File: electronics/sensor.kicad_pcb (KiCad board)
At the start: 2 copper layers, 98 x 52.8 mm, 3 parts, among them P1 SENSOR, U1 AH1815

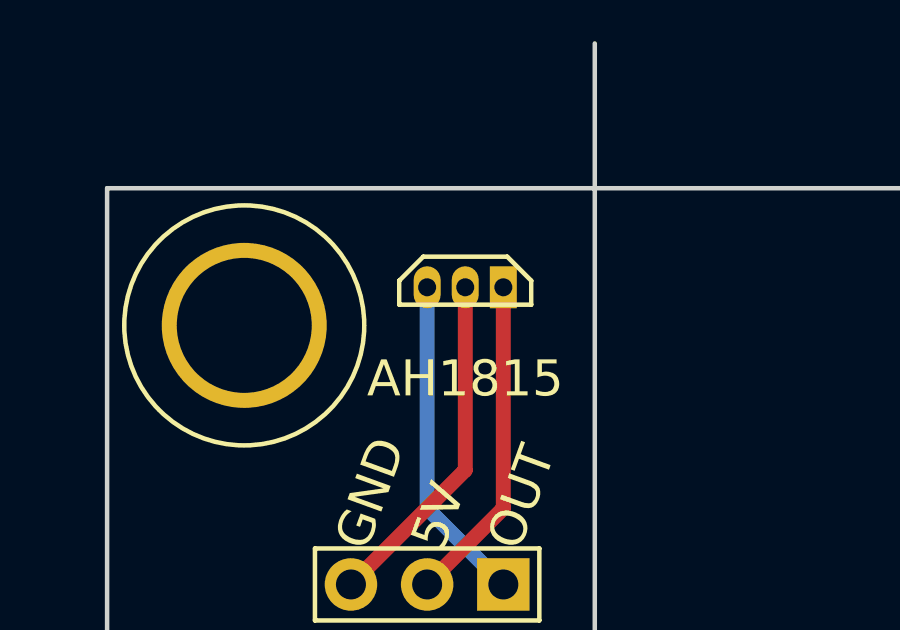
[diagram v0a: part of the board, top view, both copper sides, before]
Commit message: Replace AH1815 references with AH3391Q
The AH1815 hall effect sensor won't work, as it samples the magnetic field too infrequently for the precision needed, as mentioned in https://github.com/scottbez1/splitflap/issues/29#issuecomment-418163631

This replaces the AH1815 schematic/pcb module with a generic "hall_effect" module (since it seems most hall effect sensors have the same pinout and physical dimensions), and updates the schematic reference and BOM to specify AH3391Q as the preferred sensor. As noted in https://github.com/scottbez1/splitflap/issues/29#issuecomment-418234571 a number of other variants of hall effect sensor would also work, besides the AH3391Q, so the PCB silkscreen is now generic ("Hall Effect" instead of "AH1815"), with added pin labels for the hall effect sensor.
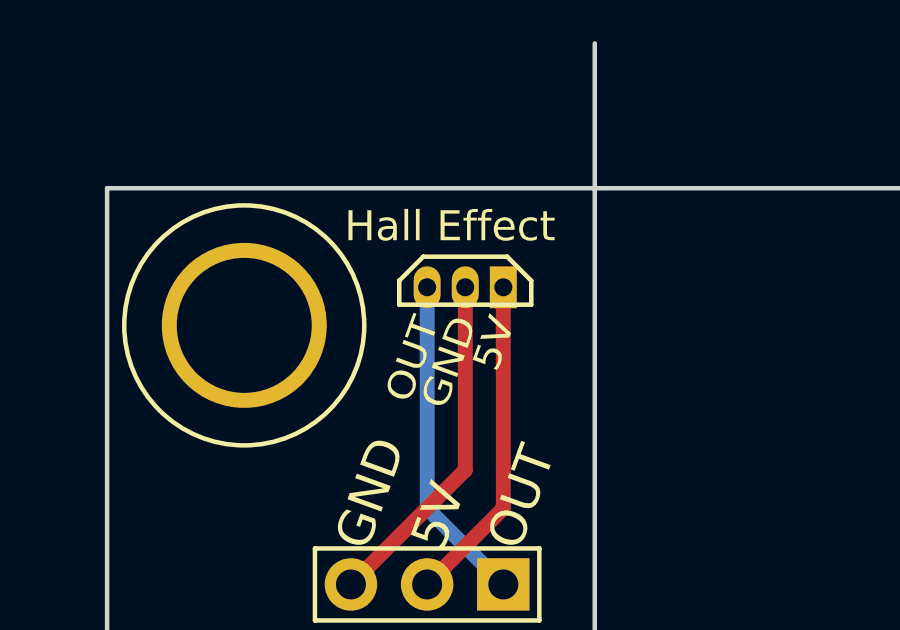
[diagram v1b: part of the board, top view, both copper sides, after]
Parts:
- U1: value AH1815 -> hall_effect; footprint ah1815:AH1815 -> hall_effect:hall_effect
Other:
- board text added: "Hall Effect"
- board text removed: "AH1815"
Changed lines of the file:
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@@
     (links 3)
     (no_connects 0)
-    (area 7.610287 15.098999 116.075001 68.075001)
+    (area 1.514287 7.37 116.075001 68.075001)
     (thickness 1.6)
-    (drawings 15)
+    (drawings 18)
     (tracks 6)
     (zones 0)
@@
       (clearance 1.5))
   )
-  (module ah1815:AH1815 (layer B.Cu)
+  (module hall_effect:hall_effect (layer B.Cu)
     (at 31.938 23.302 180)
     (fp_text reference U1 (at 5.08 1.27 180) (layer B.SilkS) hide
       (effects (font (size 1 1) (thickness 0.15)) (justify mirror))
     )
-    (fp_text value AH1815 (at 0 2.54 180) (layer B.Fab) hide
+    (fp_text value hall_effect (at 0 2.54 180) (layer B.Fab) hide
       (effects (font (size 1 1) (thickness 0.15)) (justify mirror))
     )
@@
       (net 3 "Net-(P1-Pad1)"))
   )
+  (gr_text 5V (at 33.208 24.318 70) (layer F.SilkS)
+    (effects (font (size 0.9 1) (thickness 0.15)) (justify right))
+  )
+  (gr_text GND (at 31.938 24.318 70) (layer F.SilkS)
+    (effects (font (size 0.9 1) (thickness 0.15)) (justify right))
+  )
+  (gr_text OUT (at 30.668 24.318 70) (layer F.SilkS)
+    (effects (font (size 0.9 1) (thickness 0.15)) (justify right))
+  )
   (dimension 8.636 (width 0.3) (layer Cmts.User)
     (gr_text "8.636 mm" (at 28.89 14.92) (layer Cmts.User)
@@
   )
   (gr_line (start 20 20) (end 116 20) (angle 90) (layer Edge.Cuts) (width 0.15))
-  (gr_text AH1815 (at 31.938 26.35) (layer F.SilkS)
-    (effects (font (size 1.2 1.2) (thickness 0.24)))
+  (gr_text "Hall Effect" (at 31.43 21.27) (layer F.SilkS)
+    (effects (font (size 1 1) (thickness 0.15)))
   )
   (gr_text OUT (at 33.208 31.938 70) (layer F.SilkS)

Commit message: Change sensor references to U100/P100 to avoid confusion with U1/P1 on controller PCB
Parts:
- U100: renamed from U1; value hall_effect -> AH3391Q
- renumbered P1 to P100
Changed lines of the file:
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@@
     (links 3)
     (no_connects 0)
-    (area 1.514287 7.37 116.075001 68.075001)
+    (area 17.892999 15.098999 116.075001 68.075001)
     (thickness 1.6)
     (drawings 18)
@@
   )
   (net 0 "")
-  (net 1 "Net-(P1-Pad3)")
-  (net 2 "Net-(P1-Pad2)")
-  (net 3 "Net-(P1-Pad1)")
+  (net 1 "Net-(P100-Pad1)")
+  (net 2 "Net-(P100-Pad2)")
+  (net 3 "Net-(P100-Pad3)")
   (net_class Default "This is the default net class."
     (clearance 0.2)
@@
     (uvia_dia 0.3)
     (uvia_drill 0.1)
+    (add_net "Net-(P100-Pad1)")
+    (add_net "Net-(P100-Pad2)")
+    (add_net "Net-(P100-Pad3)")
   )
   (net_class 5V ""
@@
     (uvia_dia 0.3)
     (uvia_drill 0.1)
-    (add_net "Net-(P1-Pad1)")
-    (add_net "Net-(P1-Pad2)")
-    (add_net "Net-(P1-Pad3)")
   )
   (net_class VMOT ""
@@
     (descr "Through hole pin header")
     (tags "pin header")
-    (fp_text reference P1 (at -2.032 0 360) (layer F.SilkS) hide
+    (fp_text reference P100 (at -2.032 0 360) (layer F.SilkS) hide
       (effects (font (size 1 1) (thickness 0.15)))
     )
@@
     (fp_line (start -1.2 -1.2) (end 1.2 -1.2) (layer F.SilkS) (width 0.15))
     (pad 1 thru_hole rect (at 0 0 270) (size 1.75 1.75) (drill 1) (layers *.Cu *.Mask F.SilkS)
-      (net 3 "Net-(P1-Pad1)"))
+      (net 1 "Net-(P100-Pad1)"))
     (pad 2 thru_hole circle (at 0 2.54 270) (size 1.75 1.75) (drill 1) (layers *.Cu *.Mask F.SilkS)
-      (net 2 "Net-(P1-Pad2)"))
+      (net 2 "Net-(P100-Pad2)"))
     (pad 3 thru_hole circle (at 0 5.08 270) (size 1.75 1.75) (drill 1) (layers *.Cu *.Mask F.SilkS)
-      (net 1 "Net-(P1-Pad3)"))
+      (net 3 "Net-(P100-Pad3)"))
     (model Pin_Headers.3dshapes/Pin_Header_Straight_1x03.wrl
       (at (xyz 0 -0.1 0))
@@
   (module hall_effect:hall_effect (layer B.Cu)
     (at 31.938 23.302 180)
-    (fp_text reference U1 (at 5.08 1.27 180) (layer B.SilkS) hide
+    (fp_text reference U100 (at 5.08 1.27 180) (layer B.SilkS) hide
       (effects (font (size 1 1) (thickness 0.15)) (justify mirror))
     )
-    (fp_text value hall_effect (at 0 2.54 180) (layer B.Fab) hide
+    (fp_text value AH3391Q (at 0 2.54 180) (layer B.Fab) hide
       (effects (font (size 1 1) (thickness 0.15)) (justify mirror))
     )
@@
     (fp_line (start -2.2 0.58) (end 2.2 0.58) (layer B.SilkS) (width 0.15))
     (pad 1 thru_hole rect (at -1.27 0 180) (size 0.9 1.4) (drill 0.6) (layers *.Cu *.Mask)
-      (net 2 "Net-(P1-Pad2)"))
+      (net 2 "Net-(P100-Pad2)"))
     (pad 2 thru_hole oval (at 0 0 180) (size 0.9 1.4) (drill 0.6) (layers *.Cu *.Mask)
-      (net 1 "Net-(P1-Pad3)"))
+      (net 3 "Net-(P100-Pad3)"))
     (pad 3 thru_hole oval (at 1.27 0 180) (size 0.9 1.4) (drill 0.6) (layers *.Cu *.Mask)
-      (net 3 "Net-(P1-Pad1)"))
+      (net 1 "Net-(P100-Pad1)"))
   )
   (gr_text 5V (at 33.208 24.318 70) (layer F.SilkS)
@@
   (gr_line (start 17.968 36.256) (end 73.848 36.256) (angle 90) (layer Edge.Cuts) (width 0.15))
   (gr_line (start 20 68) (end 20 20) (angle 90) (layer Edge.Cuts) (width 0.15))
-  (segment (start 31.938 23.302) (end 31.938 29.398) (width 0.5) (layer F.Cu) (net 1) (status 10))
-  (segment (start 31.938 29.398) (end 28.128 33.208) (width 0.5) (layer F.Cu) (net 1) (status 20))
+  (segment (start 33.208 33.208) (end 30.668 30.668) (width 0.5) (layer B.Cu) (net 1) (status 10))
+  (segment (start 30.668 30.668) (end 30.668 23.302) (width 0.5) (layer B.Cu) (net 1) (status 20))
   (segment (start 33.208 23.302) (end 33.208 30.668) (width 0.5) (layer F.Cu) (net 2) (status 10))
   (segment (start 33.208 30.668) (end 30.668 33.208) (width 0.5) (layer F.Cu) (net 2) (status 20))
-  (segment (start 33.208 33.208) (end 30.668 30.668) (width 0.5) (layer B.Cu) (net 3) (status 10))
-  (segment (start 30.668 30.668) (end 30.668 23.302) (width 0.5) (layer B.Cu) (net 3) (status 20))
+  (segment (start 31.938 23.302) (end 31.938 29.398) (width 0.5) (layer F.Cu) (net 3) (status 10))
+  (segment (start 31.938 29.398) (end 28.128 33.208) (width 0.5) (layer F.Cu) (net 3) (status 20))
 )

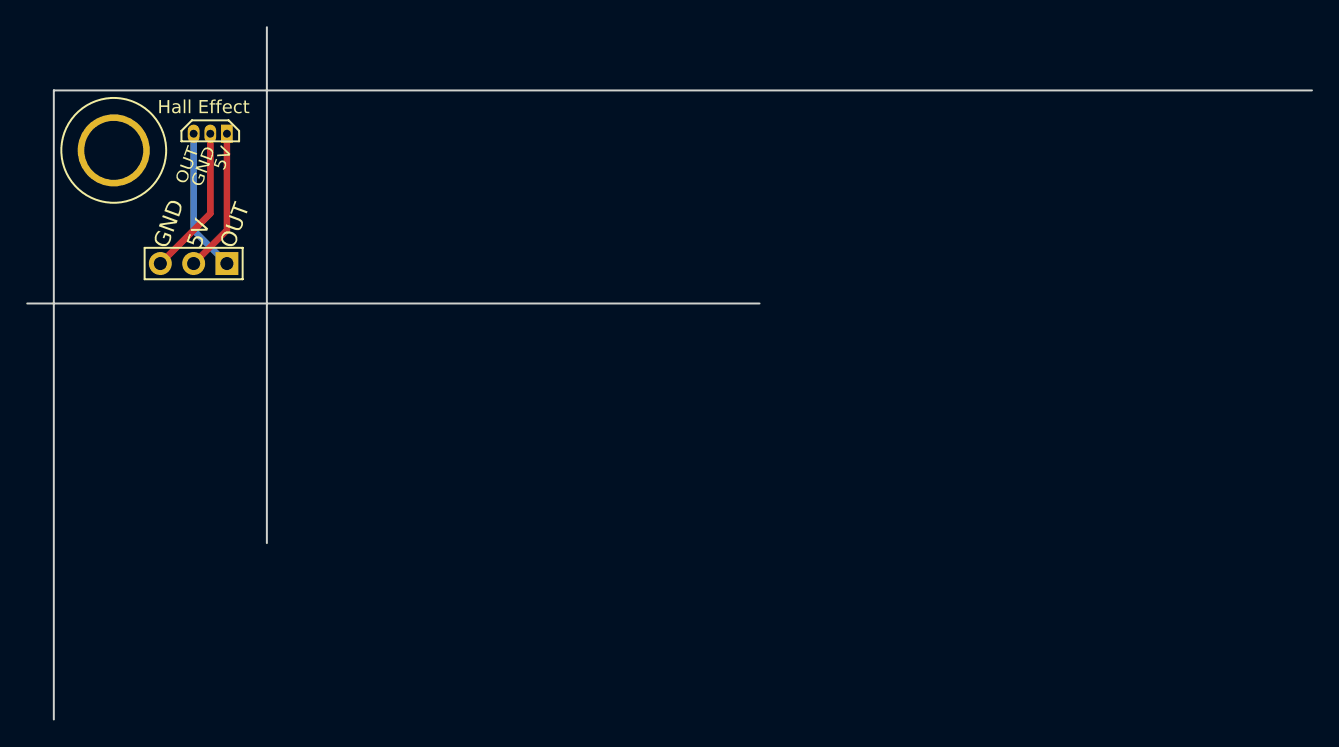
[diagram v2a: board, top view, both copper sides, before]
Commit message: Sensor PCB Tweaks (#135)
Fixes the sensor PCB `Edge.Cuts` layer continuity and moves the commit silkscreen off of the pads.

These commits were cherry-picked from PR #97
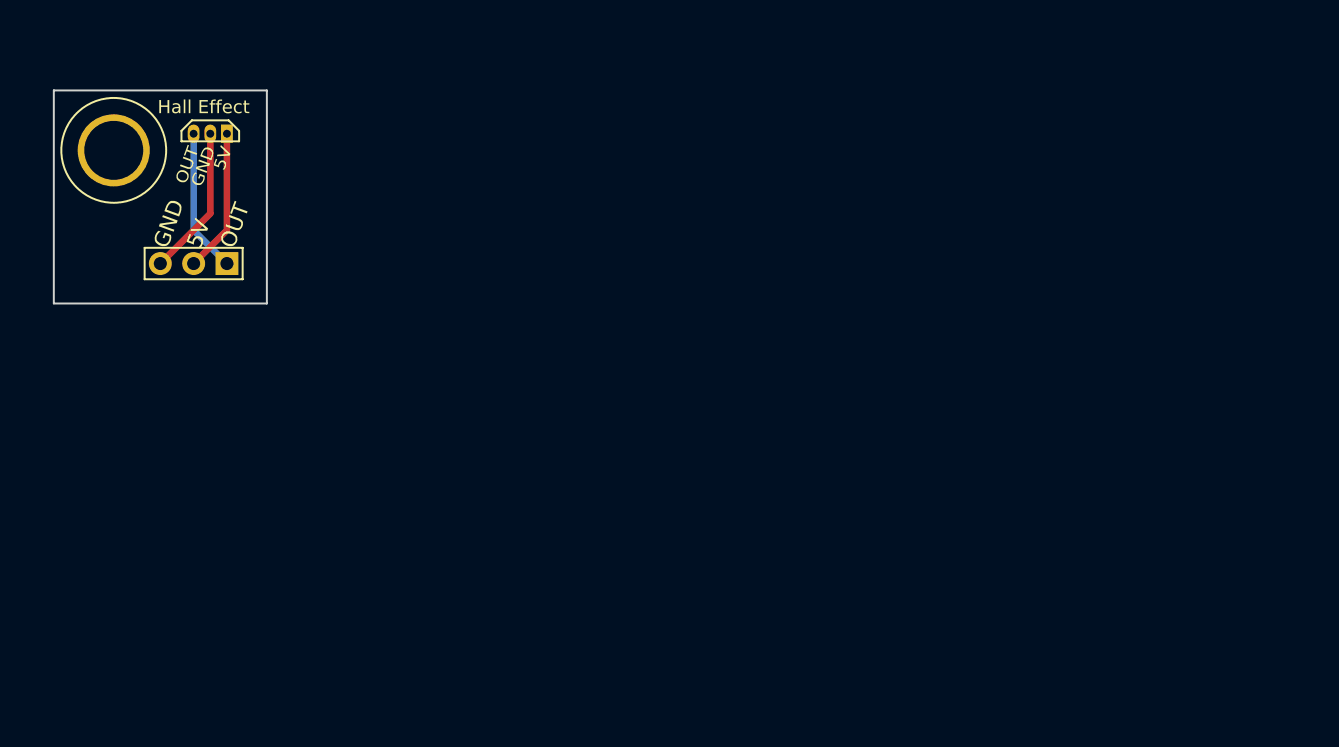
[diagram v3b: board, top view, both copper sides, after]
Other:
- board size 98 x 52.8 mm -> 16.3 x 16.3 mm
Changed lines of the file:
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@@
     (links 3)
     (no_connects 0)
-    (area 17.892999 15.098999 116.075001 68.075001)
+    (area 19.924999 19.924999 36.331001 36.331001)
     (thickness 1.6)
     (drawings 18)
@@
       (net 1 "Net-(P100-Pad1)"))
   )
+  (gr_line (start 20 36.256) (end 20 20) (angle 90) (layer Edge.Cuts) (width 0.15))
   (gr_text 5V (at 33.208 24.318 70) (layer F.SilkS)
     (effects (font (size 0.9 1) (thickness 0.15)) (justify right))
@@
     (arrow2b (pts (xy 24.572 18.476) (xy 25.698504 17.889579)))
   )
-  (gr_text "COMMIT: deadbeef\nDATE: YYYY-MM-DD" (at 35.494 31.684) (layer B.SilkS)
+  (gr_text "COMMIT: deadbeef\nDATE: YYYY-MM-DD" (at 35.494 30.25) (layer B.SilkS)
     (effects (font (size 1 0.9) (thickness 0.2)) (justify left mirror))
   )
@@
     (arrow2b (pts (xy 24.572 38.034) (xy 25.698504 37.447579)))
   )
-  (gr_line (start 20 20) (end 116 20) (angle 90) (layer Edge.Cuts) (width 0.15))
+  (gr_line (start 20 20) (end 36.256 20) (angle 90) (layer Edge.Cuts) (width 0.15))
   (gr_text "Hall Effect" (at 31.43 21.27) (layer F.SilkS)
     (effects (font (size 1 1) (thickness 0.15)))
@@
     (effects (font (size 1.2 1.2) (thickness 0.25)) (justify left))
   )
-  (gr_line (start 36.256 15.174) (end 36.256 54.544) (angle 90) (layer Edge.Cuts) (width 0.15))
-  (gr_line (start 17.968 36.256) (end 73.848 36.256) (angle 90) (layer Edge.Cuts) (width 0.15))
-  (gr_line (start 20 68) (end 20 20) (angle 90) (layer Edge.Cuts) (width 0.15))
+  (gr_line (start 36.256 20) (end 36.256 36.256) (angle 90) (layer Edge.Cuts) (width 0.15))
+  (gr_line (start 20 36.256) (end 36.256 36.256) (angle 90) (layer Edge.Cuts) (width 0.15))
   (segment (start 33.208 33.208) (end 30.668 30.668) (width 0.5) (layer B.Cu) (net 1) (status 10))
   (segment (start 30.668 30.668) (end 30.668 23.302) (width 0.5) (layer B.Cu) (net 1) (status 20))
